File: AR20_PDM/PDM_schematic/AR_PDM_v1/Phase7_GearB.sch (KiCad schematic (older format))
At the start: 10 parts, among them Q8 BTS50025-1TAD, U8 INA233

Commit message: Working on pcb layout
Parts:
- removed D?: D_Schottky_x2, symbol AR20_PDM_v1-rescue:D_Schottky_x2
- added D55, D56: D_Schottky_BAT60A, AR_PDM_v1:D_Shotky_BAT60_HandSoldering, symbol AR20_PDM_v1-rescue:D_Schottky_BAT60A
- gave numbers to parts that had none: 4
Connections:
- net GND: now also D55.2 (A), D56.2 (A)
- net at R121.1, U8.10 (IN+): now also D56.1 (K)
- net at R119.1, U8.9 (In-): now also D55.1 (K)
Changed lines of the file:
@@
 AR Path="/5E0FCFDC/5EEBF4F7" Ref="R?"  Part="1"
 AR Path="/5E0FDCCC/5EEBF4F7" Ref="R?"  Part="1"
-AR Path="/5E10174B/5EEBF4F7" Ref="R?"  Part="1"
-F 0 "R?" V 6643 1600 50  0000 C CNN
+AR Path="/5E10174B/5EEBF4F7" Ref="R120"  Part="1"
+F 0 "R120" V 6643 1600 50  0000 C CNN
 F 1 "2m_1%_4W" V 6734 1600 50  0000 C CNN
 F 2 "Resistor_SMD:R_2512_6332Metric" V 6780 1600 50  0001 C CNN
@@
 Text HLabel 7300 1600 2    50   Input ~ 10
 V+12V
-$Comp
-L AR20_PDM_v1-rescue:D_Schottky_x2 D?
-U 1 1 5EEBF4FE
-P 6950 4825
-AR Path="/5DA89415/5EEBF4FE" Ref="D?"  Part="1"
-AR Path="/5E10174B/5EEBF4FE" Ref="D?"  Part="1"
-F 0 "D?" H 6950 5041 50  0000 C CNN
-F 1 "D_Schottky_x2" H 6950 4950 50  0000 C CNN
-F 2 "" H 6950 4825 50  0001 C CNN
-F 3 "~" H 6950 4825 50  0001 C CNN
-	1    6950 4825
-	1    0    0    -1
-$EndComp
 $Comp
 L AR20_PDM_v1-rescue:R-Device R?
@@
 AR Path="/5E0FCFDC/5EEBF504" Ref="R?"  Part="1"
 AR Path="/5E0FDCCC/5EEBF504" Ref="R?"  Part="1"
-AR Path="/5E10174B/5EEBF504" Ref="R?"  Part="1"
-F 0 "R?" V 6443 3850 50  0000 C CNN
+AR Path="/5E10174B/5EEBF504" Ref="R119"  Part="1"
+F 0 "R119" V 6443 3850 50  0000 C CNN
 F 1 "1K_1%" V 6534 3850 50  0000 C CNN
 F 2 "Resistor_SMD:R_0603_1608Metric" V 6580 3850 50  0001 C CNN
@@
 AR Path="/5E0FCFDC/5EEBF50A" Ref="R?"  Part="1"
 AR Path="/5E0FDCCC/5EEBF50A" Ref="R?"  Part="1"
-AR Path="/5E10174B/5EEBF50A" Ref="R?"  Part="1"
-F 0 "R?" V 6843 3850 50  0000 C CNN
+AR Path="/5E10174B/5EEBF50A" Ref="R121"  Part="1"
+F 0 "R121" V 6843 3850 50  0000 C CNN
 F 1 "1K_1%" V 6934 3850 50  0000 C CNN
 F 2 "Resistor_SMD:R_0603_1608Metric" V 6980 3850 50  0001 C CNN
@@
 Text Notes 7075 2000 0    50   ~ 10
 Place shunt and INA233 close, \nroute togethere, differentialy pair. \nKeep short, and away from Noise.
-$Comp
-L AR20_PDM_v1-rescue:GND-power #PWR?
-U 1 1 5EEBF518
-P 6950 5025
-AR Path="/5DA89415/5EEBF518" Ref="#PWR?"  Part="1"
-AR Path="/5DEB10A1/5EEBF518" Ref="#PWR?"  Part="1"
-AR Path="/5DEB20EA/5EEBF518" Ref="#PWR?"  Part="1"
-AR Path="/5E0E4725/5EEBF518" Ref="#PWR?"  Part="1"
-AR Path="/5E0E4A93/5EEBF518" Ref="#PWR?"  Part="1"
-AR Path="/5E0E4EB5/5EEBF518" Ref="#PWR?"  Part="1"
-AR Path="/5E0E5304/5EEBF518" Ref="#PWR?"  Part="1"
-AR Path="/5E0E594B/5EEBF518" Ref="#PWR?"  Part="1"
-AR Path="/5E0E607C/5EEBF518" Ref="#PWR?"  Part="1"
-AR Path="/5E0FB5C8/5EEBF518" Ref="#PWR?"  Part="1"
-AR Path="/5E0FBBBD/5EEBF518" Ref="#PWR?"  Part="1"
-AR Path="/5E0FC3A2/5EEBF518" Ref="#PWR?"  Part="1"
-AR Path="/5E0FCFDC/5EEBF518" Ref="#PWR?"  Part="1"
-AR Path="/5E0FDCCC/5EEBF518" Ref="#PWR?"  Part="1"
-AR Path="/5E10174B/5EEBF518" Ref="#PWR?"  Part="1"
-F 0 "#PWR?" H 6950 4775 50  0001 C CNN
-F 1 "GND" H 6955 4852 50  0000 C CNN
-F 2 "" H 6950 5025 50  0001 C CNN
-F 3 "" H 6950 5025 50  0001 C CNN
-	1    6950 5025
-	1    0    0    -1
-$EndComp
 Wire Wire Line
 	4775 1600 6650 1600
@@
 Wire Wire Line
 	6650 4400 8750 4400
-Connection ~ 6650 4400
-Wire Wire Line
-	6650 4400 6650 4825
-Wire Wire Line
-	8750 4300 7250 4300
-Wire Wire Line
-	7250 4825 7250 4300
-Connection ~ 7250 4300
-Wire Wire Line
-	7250 4300 7050 4300
 $Comp
 L AR20_PDM_v1-rescue:R-Device R?
@@
 AR Path="/5E0FCFDC/5EEC877D" Ref="R?"  Part="1"
 AR Path="/5E0FDCCC/5EEC877D" Ref="R?"  Part="1"
-AR Path="/5E10174B/5EEC877D" Ref="R?"  Part="1"
-F 0 "R?" V 8093 4100 50  0000 C CNN
+AR Path="/5E10174B/5EEC877D" Ref="R122"  Part="1"
+F 0 "R122" V 8093 4100 50  0000 C CNN
 F 1 "10K" V 8184 4100 50  0000 C CNN
 F 2 "Resistor_SMD:R_0603_1608Metric" V 8230 4100 50  0001 C CNN
@@
 Text HLabel 8150 4100 0    50   Output ~ 10
 P7_OUT
+$Comp
+L AR20_PDM_v1-rescue:D_Schottky_BAT60A D?
+U 1 1 5EFB4F22
+P 6700 4775
+AR Path="/5DA89415/5EFB4F22" Ref="D?"  Part="1"
+AR Path="/5E10174B/5EFB4F22" Ref="D55"  Part="1"
+F 0 "D55" V 6530 4885 50  0000 L CNN
+F 1 "D_Schottky_BAT60A" V 6621 4885 50  0000 L CNN
+F 2 "AR_PDM_v1:D_Shotky_BAT60_HandSoldering" H 6800 4725 50  0001 C CNN
+F 3 "~" H 6800 4725 50  0001 C CNN
+	1    6700 4775
+	0    1    1    0
+$EndComp
+$Comp
+L AR20_PDM_v1-rescue:GND-power #PWR?
+U 1 1 5EFB4F28
+P 6875 4950
+AR Path="/5DA89415/5EFB4F28" Ref="#PWR?"  Part="1"
+AR Path="/5DEB10A1/5EFB4F28" Ref="#PWR?"  Part="1"
+AR Path="/5DEB20EA/5EFB4F28" Ref="#PWR?"  Part="1"
+AR Path="/5E0E4725/5EFB4F28" Ref="#PWR?"  Part="1"
+AR Path="/5E0E4A93/5EFB4F28" Ref="#PWR?"  Part="1"
+AR Path="/5E0E4EB5/5EFB4F28" Ref="#PWR?"  Part="1"
+AR Path="/5E0E5304/5EFB4F28" Ref="#PWR?"  Part="1"
+AR Path="/5E0E594B/5EFB4F28" Ref="#PWR?"  Part="1"
+AR Path="/5E0E607C/5EFB4F28" Ref="#PWR?"  Part="1"
+AR Path="/5E0FB5C8/5EFB4F28" Ref="#PWR?"  Part="1"
+AR Path="/5E0FBBBD/5EFB4F28" Ref="#PWR?"  Part="1"
+AR Path="/5E0FC3A2/5EFB4F28" Ref="#PWR?"  Part="1"
+AR Path="/5E0FCFDC/5EFB4F28" Ref="#PWR?"  Part="1"
+AR Path="/5E0FDCCC/5EFB4F28" Ref="#PWR?"  Part="1"
+AR Path="/5E10174B/5EFB4F28" Ref="#PWR023"  Part="1"
+F 0 "#PWR023" H 6875 4700 50  0001 C CNN
+F 1 "GND" H 6880 4777 50  0000 C CNN
+F 2 "" H 6875 4950 50  0001 C CNN
+F 3 "" H 6875 4950 50  0001 C CNN
+	1    6875 4950
+	1    0    0    -1
+$EndComp
+$Comp
+L AR20_PDM_v1-rescue:D_Schottky_BAT60A D?
+U 1 1 5EFB4F2E
+P 7150 4775
+AR Path="/5DA89415/5EFB4F2E" Ref="D?"  Part="1"
+AR Path="/5E10174B/5EFB4F2E" Ref="D56"  Part="1"
+F 0 "D56" V 6980 4885 50  0000 L CNN
+F 1 "D_Schottky_BAT60A" V 7071 4885 50  0000 L CNN
+F 2 "AR_PDM_v1:D_Shotky_BAT60_HandSoldering" H 7250 4725 50  0001 C CNN
+F 3 "~" H 7250 4725 50  0001 C CNN
+	1    7150 4775
+	0    1    1    0
+$EndComp
+Wire Wire Line
+	6650 4475 6650 4400
+Wire Wire Line
+	7100 4475 7100 4300
+Wire Wire Line
+	6650 4825 6875 4825
+Wire Wire Line
+	6875 4950 6875 4825
+Connection ~ 6875 4825
+Wire Wire Line
+	6875 4825 7100 4825
+Wire Wire Line
+	7050 4300 7100 4300
+Connection ~ 7100 4300
+Wire Wire Line
+	7100 4300 8750 4300
+Connection ~ 6650 4400
 $EndSCHEMATC

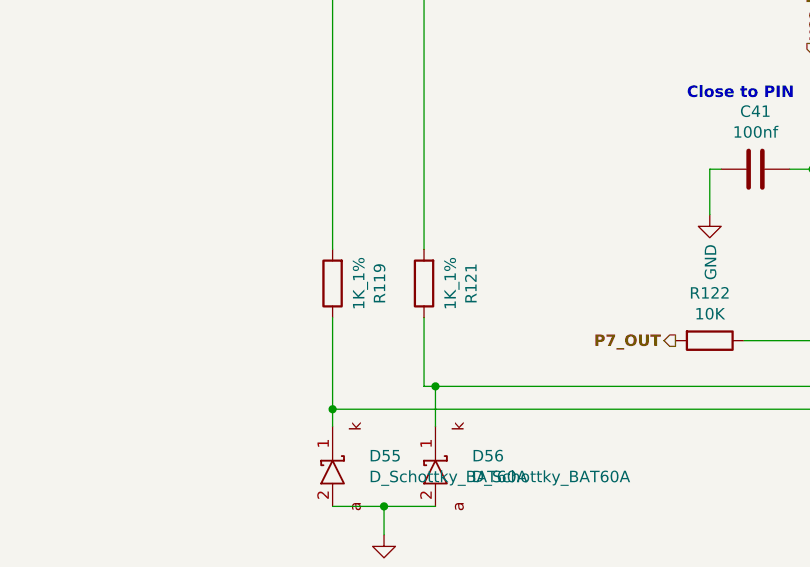
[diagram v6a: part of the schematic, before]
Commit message: shematics adjustments, and fixing values and names
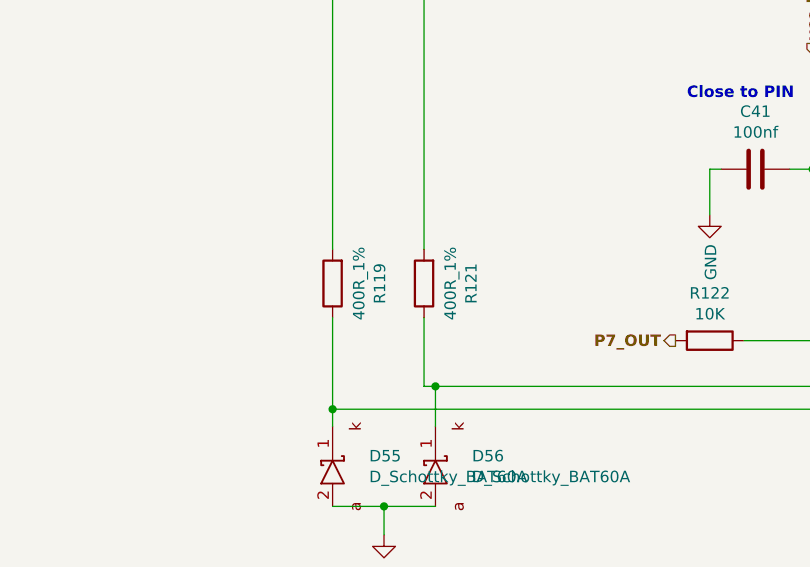
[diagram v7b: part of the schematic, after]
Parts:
- R119, R121: value 1K_1% -> 400R_1%
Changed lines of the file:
@@
 AR Path="/5E10174B/5EEBF504" Ref="R119"  Part="1"
 F 0 "R119" V 6443 3850 50  0000 C CNN
-F 1 "1K_1%" V 6534 3850 50  0000 C CNN
+F 1 "400R_1%" V 6534 3850 50  0000 C CNN
 F 2 "Resistor_SMD:R_0603_1608Metric" V 6580 3850 50  0001 C CNN
 F 3 "~" H 6650 3850 50  0001 C CNN
@@
 AR Path="/5E10174B/5EEBF50A" Ref="R121"  Part="1"
 F 0 "R121" V 6843 3850 50  0000 C CNN
-F 1 "1K_1%" V 6934 3850 50  0000 C CNN
+F 1 "400R_1%" V 6934 3850 50  0000 C CNN
 F 2 "Resistor_SMD:R_0603_1608Metric" V 6980 3850 50  0001 C CNN
 F 3 "~" H 7050 3850 50  0001 C CNN
